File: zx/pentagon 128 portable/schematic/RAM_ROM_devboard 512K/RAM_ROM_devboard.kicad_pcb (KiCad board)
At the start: 2 copper layers, 50.5 x 57.9 mm, 7 parts, among them IC1 IS61C5128AS-25TLI, J1 Conn_02x14_Odd_Even, J2 8432-11B1-RK-TP, J3 Conn_02x08_Odd_Even, J4 Conn_02x04_Odd_Even, J6 Conn_02x06_Odd_Even, J7 Conn_02x08_Odd_Even

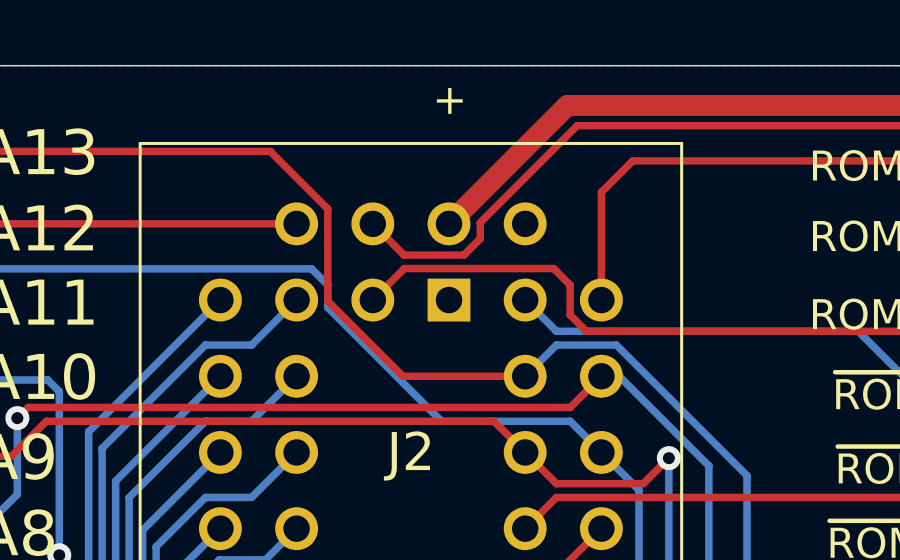
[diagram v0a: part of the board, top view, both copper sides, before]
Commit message: added z80 pdip. updated all boards
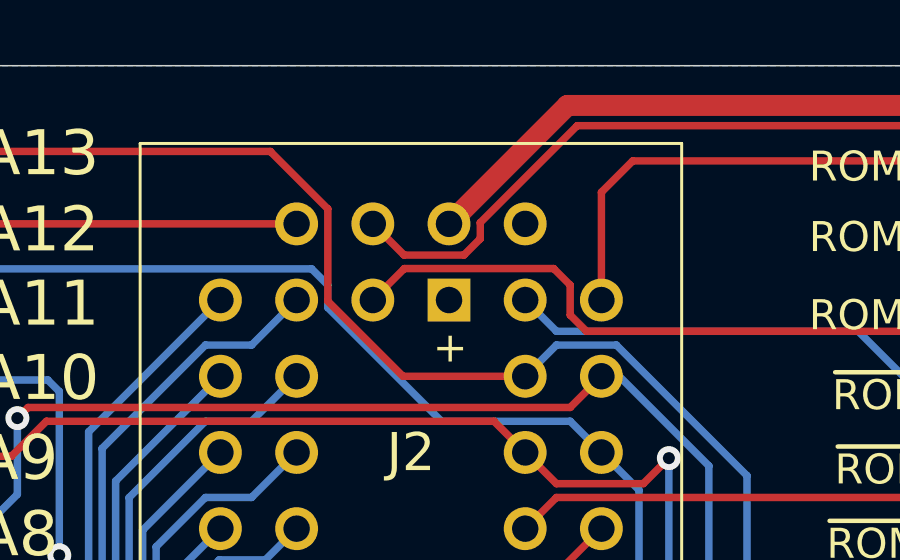
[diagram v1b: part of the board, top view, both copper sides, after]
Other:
- board text added: "JLCJLCJLCJLC"
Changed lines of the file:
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@@
   (general
     (thickness 1.6)
-    (drawings 46)
+    (drawings 47)
     (tracks 380)
     (zones 0)
@@
       (outputformat 1)
       (mirror false)
-      (drillshape 1)
+      (drillshape 0)
       (scaleselection 1)
-      (outputdirectory ""))
+      (outputdirectory "gerber/"))
   )
   (net 0 "")
@@
       (effects (font (size 1 1) (thickness 0.15)))
     )
-    (fp_text user %R (at 1.27 8.89 90) (layer F.Fab)
-      (effects (font (size 1 1) (thickness 0.15)))
-    )
     (fp_line (start 0 -1.27) (end 3.81 -1.27) (layer F.Fab) (width 0.1))
     (fp_line (start 3.81 -1.27) (end 3.81 19.05) (layer F.Fab) (width 0.1))
@@
     (fp_line (start 4.35 19.55) (end 4.35 -1.8) (layer F.CrtYd) (width 0.05))
     (fp_line (start 4.35 -1.8) (end -1.8 -1.8) (layer F.CrtYd) (width 0.05))
+    (fp_text user %R (at 1.27 8.89 90) (layer F.Fab)
+      (effects (font (size 1 1) (thickness 0.15)))
+    )
     (pad 16 thru_hole oval (at 2.54 17.78 180) (size 1.7 1.7) (drill 1) (layers *.Cu *.Mask)
       (net 3 /~RAM_WE))
@@
       (effects (font (size 1.27 1.27) (thickness 0.254)))
     )
-    (fp_text user %R (at 0 0) (layer F.Fab)
-      (effects (font (size 1.27 1.27) (thickness 0.254)))
-    )
     (fp_line (start -6.625 -10.79) (end 6.625 -10.79) (layer F.CrtYd) (width 0.05))
     (fp_line (start 6.625 -10.79) (end 6.625 10.79) (layer F.CrtYd) (width 0.05))
@@
     (fp_line (start -4.73 10.475) (end -4.73 -10.475) (layer F.SilkS) (width 0.2))
     (fp_line (start -6.375 -10.2) (end -5.08 -10.2) (layer F.SilkS) (width 0.2))
+    (fp_text user %R (at 0 0) (layer F.Fab)
+      (effects (font (size 1.27 1.27) (thickness 0.254)))
+    )
     (pad 32 smd rect (at 5.728 -9.525 90) (size 0.65 1.295) (layers F.Cu F.Paste F.Mask)
       (net 1 +5V))
@@
     )
   )
+  (gr_text JLCJLCJLCJLC (at 103.0605 110.2995) (layer B.SilkS)
+    (effects (font (size 1 1) (thickness 0.15)) (justify mirror))
+  )
   (gr_text RAM_A18 (at 135.4455 106.68) (layer F.SilkS)
     (effects (font (size 1 1) (thickness 0.15)))
@@
     (effects (font (size 1 1) (thickness 0.15)))
   )
-  (gr_text + (at 120.015 65.151) (layer F.SilkS)
+  (gr_text + (at 120.0277 73.406) (layer F.SilkS)
     (effects (font (size 1 1) (thickness 0.15)))
   )
@@
   (segment (start 143.383 94.234) (end 141.982999 95.634001) (width 0.7) (layer F.Cu) (net 1))
   (segment (start 141.982999 95.634001) (end 140.170999 95.634001) (width 0.7) (layer F.Cu) (net 1))
+  (segment (start 125.603 91.059) (end 124.6 91.059) (width 0.7) (layer F.Cu) (net 1))
+  (segment (start 135.595998 91.059) (end 125.603 91.059) (width 0.7) (layer F.Cu) (net 1))
+  (segment (start 140.170999 95.634001) (end 135.595998 91.059) (width 0.7) (layer F.Cu) (net 1))
+  (segment (start 124.6 92.329) (end 133.731 92.329) (width 0.25) (layer F.Cu) (net 2))
+  (segment (start 133.731 92.329) (end 133.731 92.329) (width 0.25) (layer F.Cu) (net 2))
+  (via (at 133.731 92.329) (size 0.8) (drill 0.4) (layers F.Cu B.Cu) (net 2))
+  (segment (start 133.731 107.061) (end 140.716 114.046) (width 0.25) (layer B.Cu) (net 2))
+  (segment (start 133.731 92.329) (end 133.731 107.061) (width 0.25) (layer B.Cu) (net 2))
+  (segment (start 140.716 114.046) (end 143.256 114.046) (width 0.7) (layer F.Cu) (net 2))
+  (segment (start 136.779 94.869) (end 140.716 98.806) (width 0.25) (layer F.Cu) (net 3))
+  (segment (start 124.6 94.869) (end 136.779 94.869) (width 0.25) (layer F.Cu) (net 3))
+  (segment (start 140.716 98.806) (end 143.256 98.806) (width 0.7) (layer F.Cu) (net 3))
   (segment (start 115.948501 68.780799) (end 114.033202 66.8655) (width 0.25) (layer F.Cu) (net 4))
   (segment (start 114.033202 66.8655) (end 102.2985 66.8655) (width 0.25) (layer F.Cu) (net 4))
@@
   (segment (start 129.921 84.6455) (end 129.921 77.673298) (width 0.25) (layer B.Cu) (net 4))
   (segment (start 99.7585 66.8655) (end 102.2985 66.8655) (width 0.7) (layer F.Cu) (net 4))
+  (segment (start 129.921 84.6455) (end 129.660502 84.6455) (width 0.25) (layer F.Cu) (net 4))
+  (segment (start 129.259499 85.307001) (end 129.921 84.6455) (width 0.25) (layer F.Cu) (net 4))
+  (segment (start 124.6 96.139) (end 124.2775 96.139) (width 0.25) (layer F.Cu) (net 4))
+  (segment (start 124.2775 96.139) (end 122.2375 94.099) (width 0.25) (layer F.Cu) (net 4))
+  (segment (start 128.794497 85.307001) (end 129.259499 85.307001) (width 0.25) (layer F.Cu) (net 4))
+  (segment (start 122.2375 94.099) (end 122.2375 91.863998) (width 0.25) (layer F.Cu) (net 4))
+  (segment (start 122.2375 91.863998) (end 128.794497 85.307001) (width 0.25) (layer F.Cu) (net 4))
   (segment (start 124.028499 75.400001) (end 105.955999 75.400001) (width 0.25) (layer F.Cu) (net 5))
   (segment (start 125.0685 74.36) (end 124.028499 75.400001) (width 0.25) (layer F.Cu) (net 5))
@@
   (segment (start 128.651 84.582) (end 128.651 77.349498) (width 0.25) (layer B.Cu) (net 5))
   (segment (start 99.7585 79.5655) (end 102.2985 79.5655) (width 0.7) (layer F.Cu) (net 5))
+  (segment (start 124.312498 97.409) (end 124.6 97.409) (width 0.25) (layer F.Cu) (net 5))
+  (segment (start 128.651 84.582) (end 127.254 85.979) (width 0.25) (layer F.Cu) (net 5))
+  (segment (start 126.930002 85.979) (end 121.67702 91.231982) (width 0.25) (layer F.Cu) (net 5))
+  (segment (start 127.254 85.979) (end 126.930002 85.979) (width 0.25) (layer F.Cu) (net 5))
+  (segment (start 121.67702 91.231982) (end 121.67702 94.773522) (width 0.25) (layer F.Cu) (net 5))
+  (segment (start 121.67702 94.773522) (end 124.312498 97.409) (width 0.25) (layer F.Cu) (net 5))
   (segment (start 105.403502 77.0255) (end 102.2985 77.0255) (width 0.25) (layer F.Cu) (net 6))
   (segment (start 121.488499 75.859999) (end 106.569003 75.859999) (width 0.25) (layer F.Cu) (net 6))
@@
   (segment (start 127.3175 77.089) (end 126.466499 77.940001) (width 0.25) (layer F.Cu) (net 6))
   (segment (start 99.7585 77.0255) (end 102.2985 77.0255) (width 0.7) (layer F.Cu) (net 6))
+  (segment (start 124.312498 98.679) (end 124.6 98.679) (width 0.25) (layer F.Cu) (net 6))
+  (segment (start 121.22701 95.593512) (end 124.312498 98.679) (width 0.25) (layer F.Cu) (net 6))
+  (segment (start 121.22701 90.157992) (end 121.22701 95.593512) (width 0.25) (layer F.Cu) (net 6))
+  (segment (start 126.866502 84.5185) (end 121.22701 90.157992) (width 0.25) (layer F.Cu) (net 6))
+  (segment (start 127.3175 84.5185) (end 126.866502 84.5185) (width 0.25) (layer F.Cu) (net 6))
   (segment (start 103.464001 70.779999) (end 102.2985 71.9455) (width 0.25) (layer B.Cu) (net 7))
   (segment (start 115.948501 71.320799) (end 115.407701 70.779999) (width 0.25) (layer B.Cu) (net 7))
@@
   (segment (start 125.9205 84.3915) (end 126.320499 83.991501) (width 0.25) (layer B.Cu) (net 7))
   (segment (start 99.7585 71.9455) (end 102.2985 71.9455) (width 0.7) (layer F.Cu) (net 7))
-  (segment (start 125.603 91.059) (end 124.6 91.059) (width 0.7) (layer F.Cu) (net 1))
-  (segment (start 135.595998 91.059) (end 125.603 91.059) (width 0.7) (layer F.Cu) (net 1))
-  (segment (start 140.170999 95.634001) (end 135.595998 91.059) (width 0.7) (layer F.Cu) (net 1))
-  (segment (start 124.6 92.329) (end 133.731 92.329) (width 0.25) (layer F.Cu) (net 2))
-  (segment (start 133.731 92.329) (end 133.731 92.329) (width 0.25) (layer F.Cu) (net 2))
-  (via (at 133.731 92.329) (size 0.8) (drill 0.4) (layers F.Cu B.Cu) (net 2))
-  (segment (start 133.731 107.061) (end 140.716 114.046) (width 0.25) (layer B.Cu) (net 2))
-  (segment (start 133.731 92.329) (end 133.731 107.061) (width 0.25) (layer B.Cu) (net 2))
-  (segment (start 140.716 114.046) (end 143.256 114.046) (width 0.7) (layer F.Cu) (net 2))
-  (segment (start 136.779 94.869) (end 140.716 98.806) (width 0.25) (layer F.Cu) (net 3))
-  (segment (start 124.6 94.869) (end 136.779 94.869) (width 0.25) (layer F.Cu) (net 3))
-  (segment (start 140.716 98.806) (end 143.256 98.806) (width 0.7) (layer F.Cu) (net 3))
-  (segment (start 129.921 84.6455) (end 129.660502 84.6455) (width 0.25) (layer F.Cu) (net 4))
-  (segment (start 129.259499 85.307001) (end 129.921 84.6455) (width 0.25) (layer F.Cu) (net 4))
-  (segment (start 124.6 96.139) (end 124.2775 96.139) (width 0.25) (layer F.Cu) (net 4))
-  (segment (start 124.2775 96.139) (end 122.2375 94.099) (width 0.25) (layer F.Cu) (net 4))
-  (segment (start 128.794497 85.307001) (end 129.259499 85.307001) (width 0.25) (layer F.Cu) (net 4))
-  (segment (start 122.2375 94.099) (end 122.2375 91.863998) (width 0.25) (layer F.Cu) (net 4))
-  (segment (start 122.2375 91.863998) (end 128.794497 85.307001) (width 0.25) (layer F.Cu) (net 4))
-  (segment (start 124.312498 97.409) (end 124.6 97.409) (width 0.25) (layer F.Cu) (net 5))
-  (segment (start 128.651 84.582) (end 127.254 85.979) (width 0.25) (layer F.Cu) (net 5))
-  (segment (start 126.930002 85.979) (end 121.67702 91.231982) (width 0.25) (layer F.Cu) (net 5))
-  (segment (start 127.254 85.979) (end 126.930002 85.979) (width 0.25) (layer F.Cu) (net 5))
-  (segment (start 121.67702 91.231982) (end 121.67702 94.773522) (width 0.25) (layer F.Cu) (net 5))
-  (segment (start 121.67702 94.773522) (end 124.312498 97.409) (width 0.25) (layer F.Cu) (net 5))
-  (segment (start 124.312498 98.679) (end 124.6 98.679) (width 0.25) (layer F.Cu) (net 6))
-  (segment (start 121.22701 95.593512) (end 124.312498 98.679) (width 0.25) (layer F.Cu) (net 6))
-  (segment (start 121.22701 90.157992) (end 121.22701 95.593512) (width 0.25) (layer F.Cu) (net 6))
-  (segment (start 126.866502 84.5185) (end 121.22701 90.157992) (width 0.25) (layer F.Cu) (net 6))
-  (segment (start 127.3175 84.5185) (end 126.866502 84.5185) (width 0.25) (layer F.Cu) (net 6))
   (segment (start 124.312498 99.949) (end 124.6 99.949) (width 0.25) (layer F.Cu) (net 7))
   (segment (start 120.777 96.413502) (end 124.312498 99.949) (width 0.25) (layer F.Cu) (net 7))
